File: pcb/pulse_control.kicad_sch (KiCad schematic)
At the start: 1 part

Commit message: WiP level control
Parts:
- added C1: 0.1uF, symbol Device:C
- added D1: BAV23CLT1G, symbol Diode:BAV70
- added D2: SMAJ13A, Diode_SMD:D_SMA, symbol Diode:SMAJ13A
- added Q1, Q2: IRLML6344, symbol Device:Q_NMOS_GSD
- added R10, R11: 180, symbol Device:R
- added R12: 8mOhm / 0.5W, symbol Device:R
- added U8: INA180A2, Package_TO_SOT_SMD:SOT-23-5, symbol Amplifier_Current:INA180A2
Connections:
- net PLS_B: now also R11.1
- net at TR2.1: now also D1.2 (A), Q2.3 (D)
- net at TR2.2: now also D2.2 (A2), R12.1, U8.4 (-)
- net at TR2.3: now also D1.1 (A), Q1.3 (D)
- new net: D1.3 (K), D2.1 (A1)
- new net: Q2.1 (G), R10.2
- new net: Q1.1 (G), R11.2
- new net: R12.2, U8.3 (+)
- new net +3V0: C1.1, U8.5 (V+)
- new net CUR: U8.1
- new net GND: C1.2, Q1.2 (S), Q2.2 (S), U8.2 (GND)
- new net PLS_T: R10.1
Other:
- note added: "7.5A max current sense"

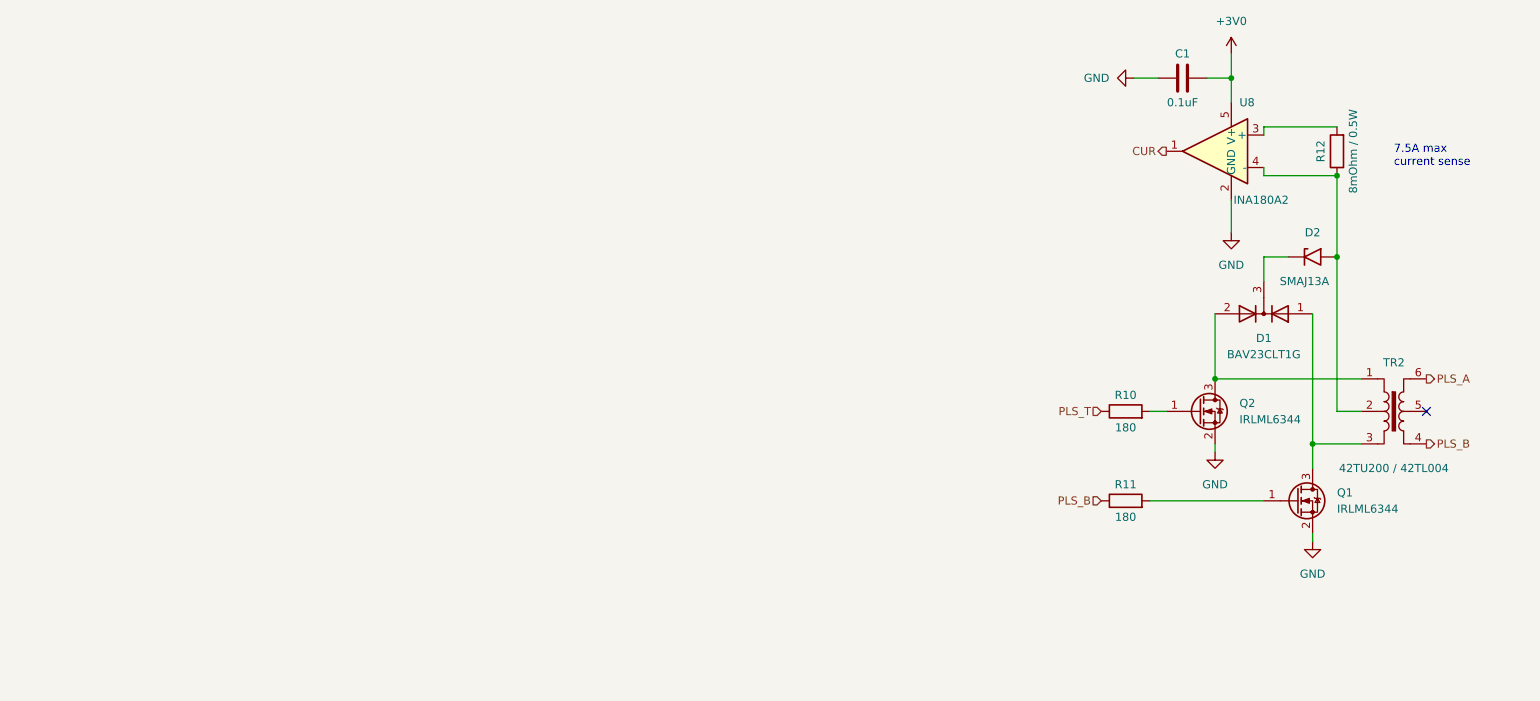
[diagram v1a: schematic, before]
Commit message: Added pulse control harmonized resistor values
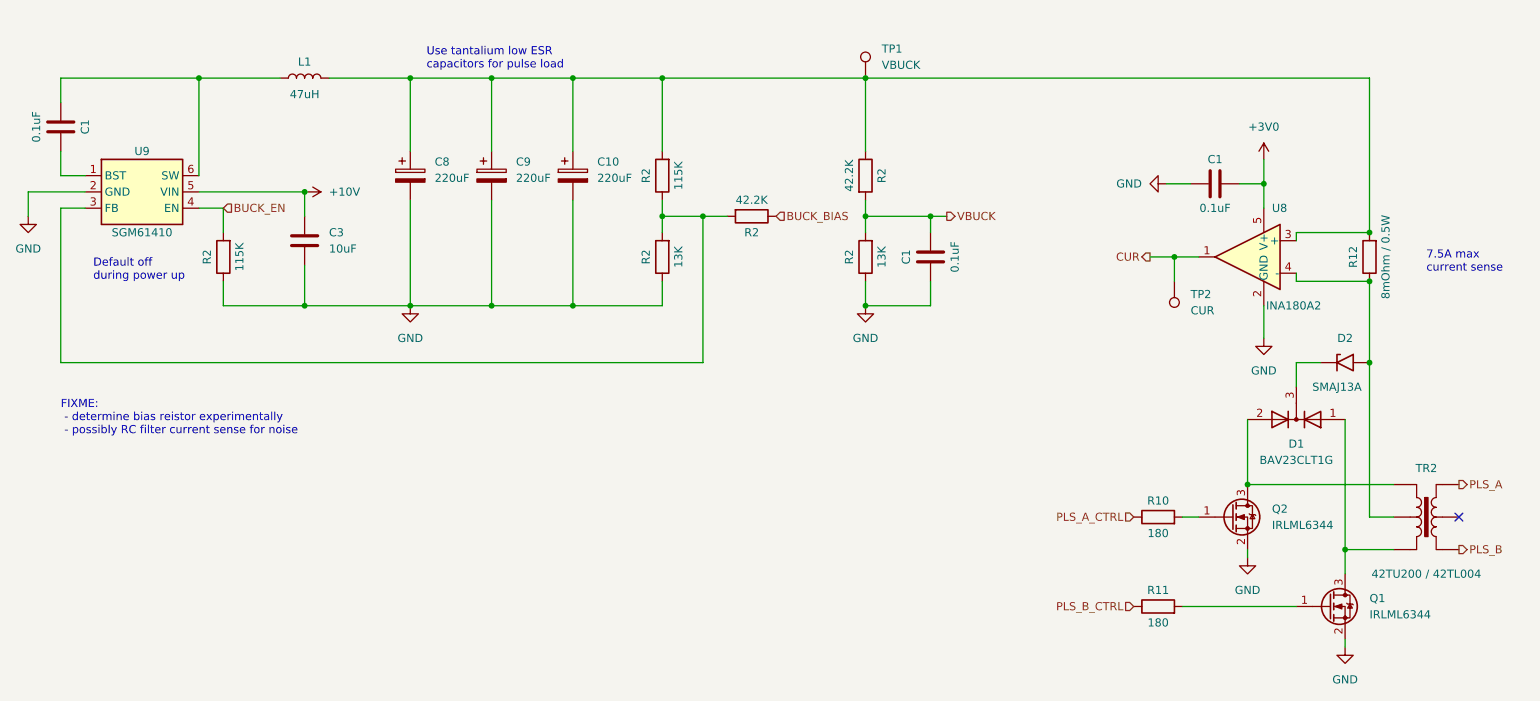
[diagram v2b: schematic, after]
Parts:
- added C1 (x2): 0.1uF, symbol Device:C
- added C10, C8, C9: 220uF, symbol Device:C_Polarized
- added C3: 10uF, symbol Device:C
- added L1: 47uH, symbol Device:L
- added R2 (x2): 115K, symbol Device:R
- added R2 (x2): 13K, symbol Device:R
- added R2 (x2): 42.2K, symbol Device:R
- added TP1: VBUCK, symbol Connector:TestPoint
- added TP2: CUR, symbol Connector:TestPoint
- added U9: SGM61410, Package_TO_SOT_SMD:TSOT-23-6, symbol sgm61410:SGM61410
- D1: footprint (none) -> Package_TO_SOT_SMD:SOT-23
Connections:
- net CUR: now also TP2.1
- net GND: now also C1.2, C10.2, C3.2, C8.2, C9.2, R2.1, R2.1, R2.1, U9.2 (GND)
- net PLS_B: no longer R11.1
- net at R12.2, U8.3 (+): now also C10.1, C8.1, C9.1, L1.2, R2.1, R2.2, TP1.1
- net PLS_T renamed PLS_A_CTRL
- new net: R2.1, R2.2, R2.2, U9.3 (FB)
- new net: C1.1, U9.1 (BST)
- new net: C1.2, L1.1, U9.6 (SW)
- new net +10V: C3.1, U9.5 (VIN)
- new net BUCK_BIAS: R2.1
- new net BUCK_EN: R2.2, U9.4 (EN)
- new net PLS_B_CTRL: R11.1
- new net VBUCK: C1.1, R2.2, R2.2
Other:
- note added: "Default off during power up"
- note added: "FIXME: - determine bias reistor experimentally - possibly RC filter current sense for noise"
- note added: "Use tantalium low ESR capacitors for pulse load"
- moved on the sheet: C1, D1, D2, Q1, Q2, R10, R11, R12, U8
